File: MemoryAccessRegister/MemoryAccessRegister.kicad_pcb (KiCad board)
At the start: 2 copper layers, 84.3 x 39.2 mm, 26 parts, among them J1 Conn_01x05_Pin, J2 Conn_01x06_Pin, J3 Conn_01x03_Pin, SW1 SW_SPDT, U1 SN74AC14N, U2 CD74HCT258E, U4 74LS173

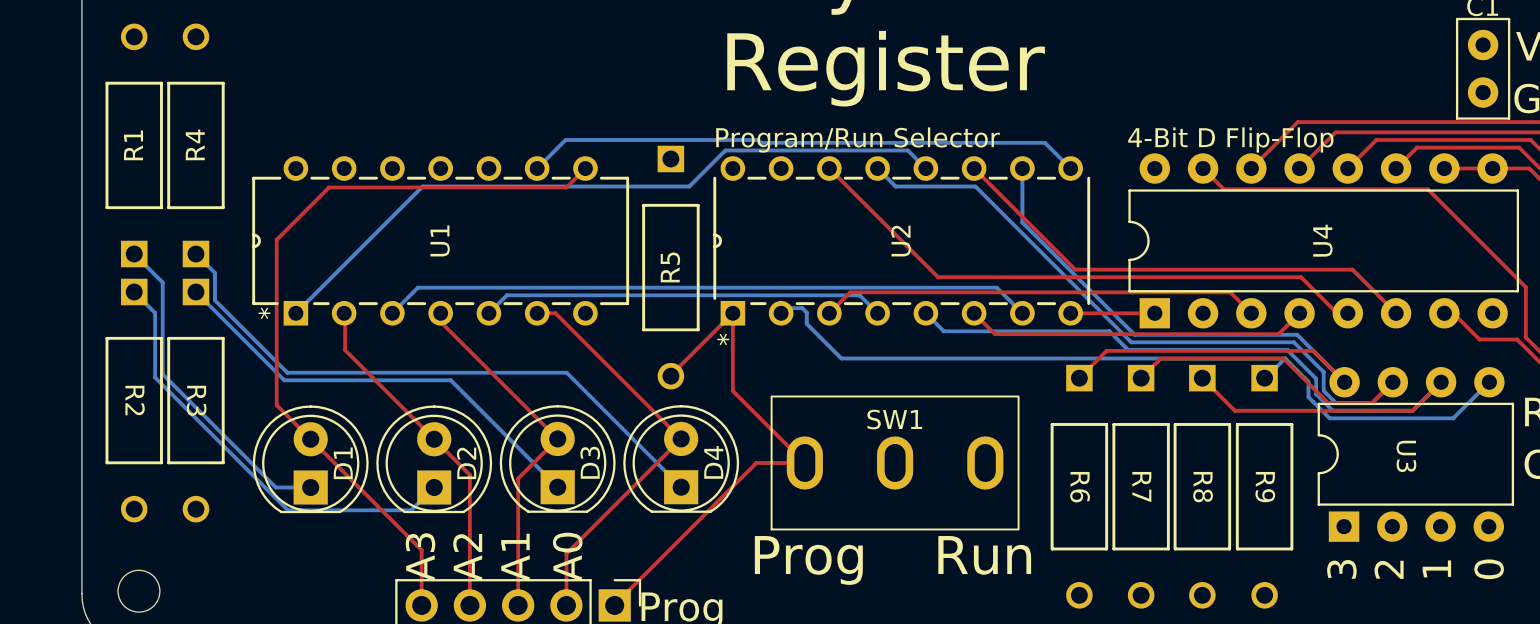
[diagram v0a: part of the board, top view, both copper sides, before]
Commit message: Minor silkscreen fixes
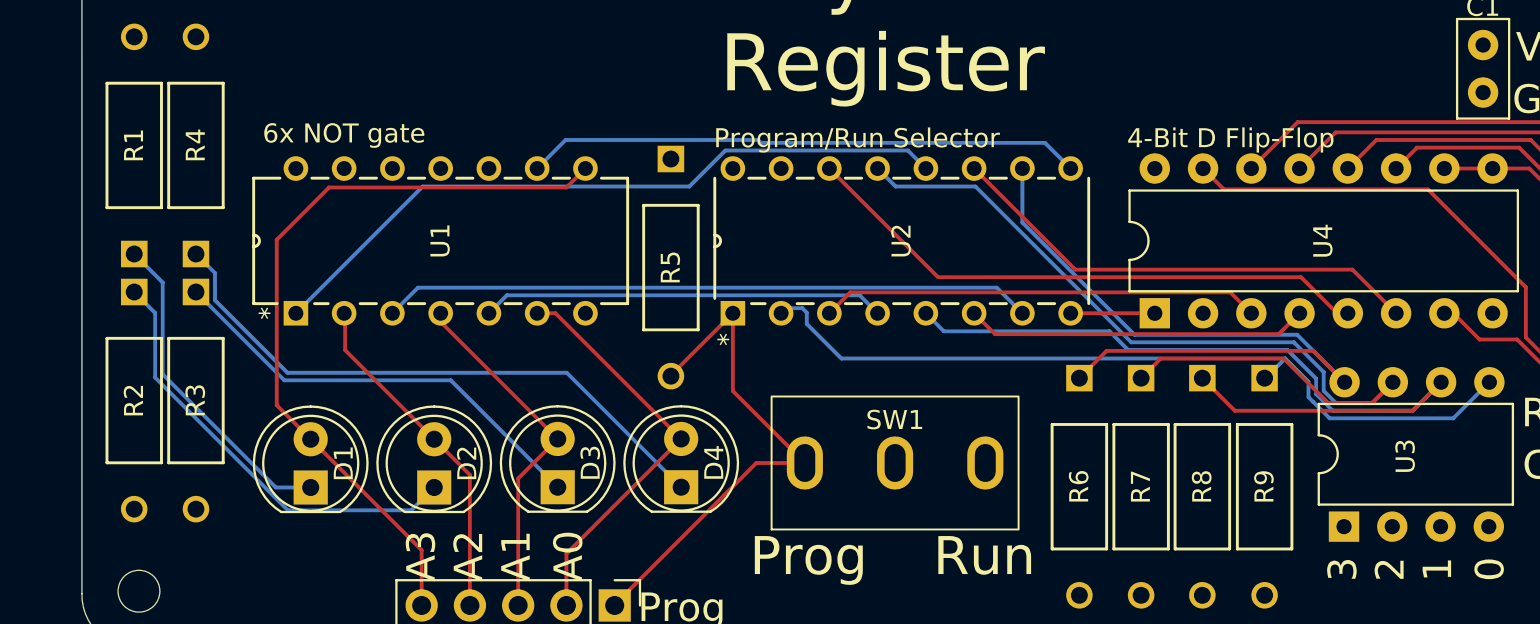
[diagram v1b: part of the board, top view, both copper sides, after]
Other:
- board text added: "6x NOT gate"
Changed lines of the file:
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@@
 		(tags "CF14JT10K0 ")
 		(property "Reference" "R2"
-			(at 5.715 0 -90)
+			(at 5.715 0 90)
 			(unlocked yes)
 			(layer "F.SilkS")
@@
 		(tags "CF14JT10K0 ")
 		(property "Reference" "R9"
-			(at 5.715 0 -90)
+			(at 5.715 0 90)
 			(unlocked yes)
 			(layer "F.SilkS")
@@
 		)
 		(fp_text user "${REFERENCE}"
-			(at 5.715 0 -90)
+			(at 5.715 0 90)
 			(unlocked yes)
 			(layer "F.Fab")
@@
 		(tags "CF14JT10K0 ")
 		(property "Reference" "R7"
-			(at 5.715 0 -90)
+			(at 5.715 0 90)
 			(unlocked yes)
 			(layer "F.SilkS")
@@
 		)
 		(fp_text user "${REFERENCE}"
-			(at 5.715 0 -90)
+			(at 5.715 0 90)
 			(unlocked yes)
 			(layer "F.Fab")
@@
 		(at 218.68 92.4 90)
 		(property "Reference" "U3"
-			(at 0 0 -90)
+			(at 0 0 90)
 			(unlocked yes)
 			(layer "F.SilkS")
@@
 		)
 		(fp_text user "${REFERENCE}"
-			(at 0 0 -90)
+			(at 0 0 90)
 			(unlocked yes)
 			(layer "F.Fab")
@@
 		(tags "CF14JT10K0 ")
 		(property "Reference" "R8"
-			(at 5.715 0 -90)
+			(at 5.715 0 90)
 			(unlocked yes)
 			(layer "F.SilkS")
@@
 		)
 		(fp_text user "${REFERENCE}"
-			(at 5.715 0 -90)
+			(at 5.715 0 90)
 			(unlocked yes)
 			(layer "F.Fab")
@@
 		(tags "CF14JT10K0 ")
 		(property "Reference" "R3"
-			(at 5.715 0 -90)
+			(at 5.715 0 90)
 			(unlocked yes)
 			(layer "F.SilkS")
@@
 		(tags "CF14JT10K0 ")
 		(property "Reference" "R6"
-			(at 5.715 0 -90)
+			(at 5.715 0 90)
 			(unlocked yes)
 			(layer "F.SilkS")
@@
 			)
 			(justify left bottom)
+		)
+	)
+	(gr_text "6x NOT gate"
+		(at 158.5 76 0)
+		(layer "F.SilkS")
+		(effects
+			(font
+				(size 1 1)
+				(thickness 0.1)
+			)
+			(justify left bottom)
